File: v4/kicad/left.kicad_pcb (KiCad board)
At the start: 2 copper layers, 158.5 x 119.3 mm, 68 parts

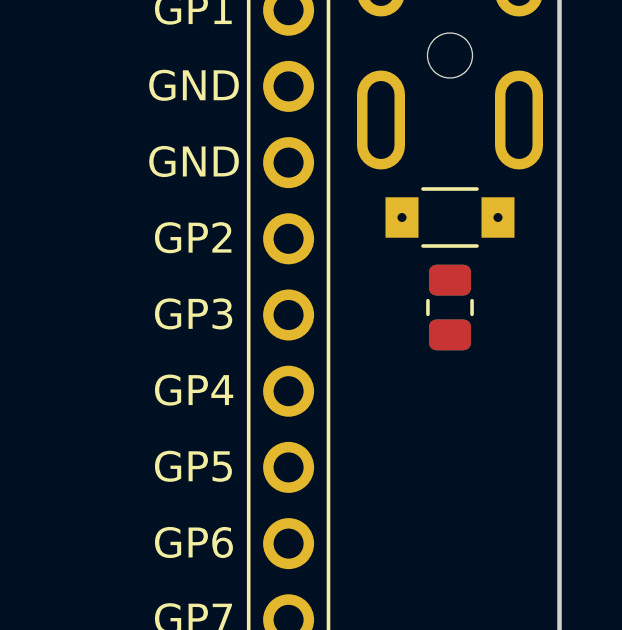
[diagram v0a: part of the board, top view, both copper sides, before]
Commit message: Finalize v4 TRRS protection placement clearance
Move data_resistor down 0.5mm (shift_y 15-17 -> 15-17.5, both halves) so
the TVS<->resistor courtyard gap is 0.67mm (was 0.17mm after the sod-123fl
land-pattern update grew the TVS courtyard). All clearances verified: TVS
0.75mm from the jack, ~28mm of open board below, both parts within the
outline. Regenerate and re-sync v4/kicad.
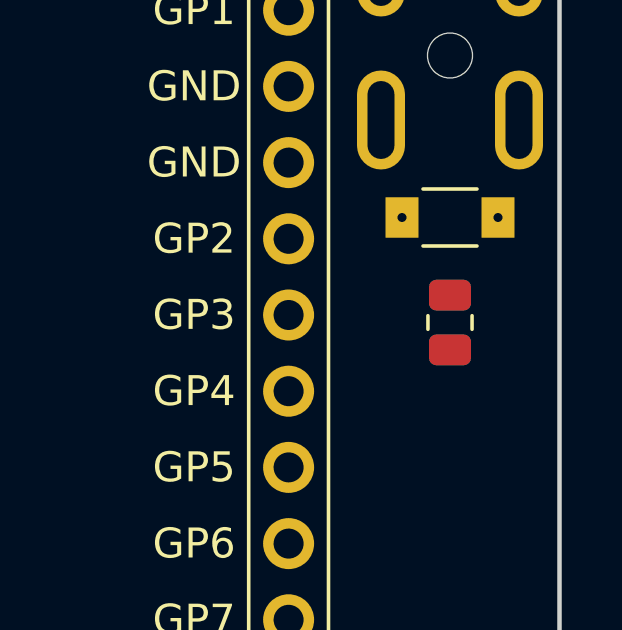
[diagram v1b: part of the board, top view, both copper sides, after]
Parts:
- moved SMD1 0.50 mm to (194.8, 118.0)

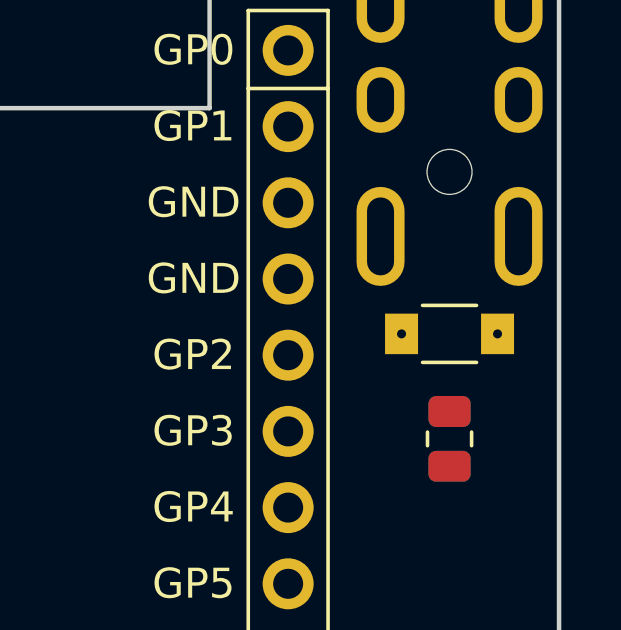
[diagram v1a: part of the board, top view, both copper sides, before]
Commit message: Label v4 TRRS protection parts descriptively
TVS (sod-123fl): name pads K (cathode/'to') and A (anode/'from') instead
of 1/2, set the value to SMF3.3CA, and document the params/pads in comments.
Resistor (smd_0805): override designator to R (R1, not the generic SMD1)
and add a '100R' silk value label. Document each part's pad->net mapping
in the ergogen config comments.
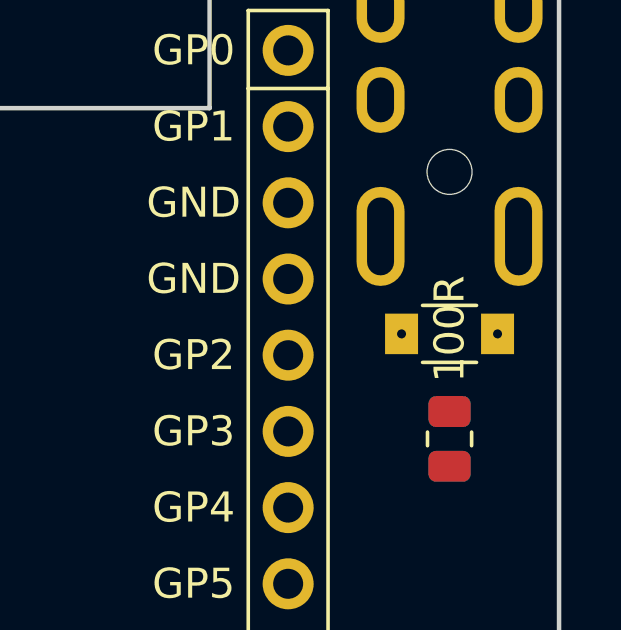
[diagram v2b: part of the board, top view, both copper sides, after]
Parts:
- removed SMD1: , smd_805
- added R1: , smd_805, F.Cu at (194.8, 118.0)
- D31: value SOD-123FL -> SMF3.3CA

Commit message: Sync v4 kicad working PCBs with finalized TRRS protection placement
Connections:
- TRRS1 pad 2: DATA_RAW -> GND
- TRRS1 pad 3: GND -> DATA_RAW

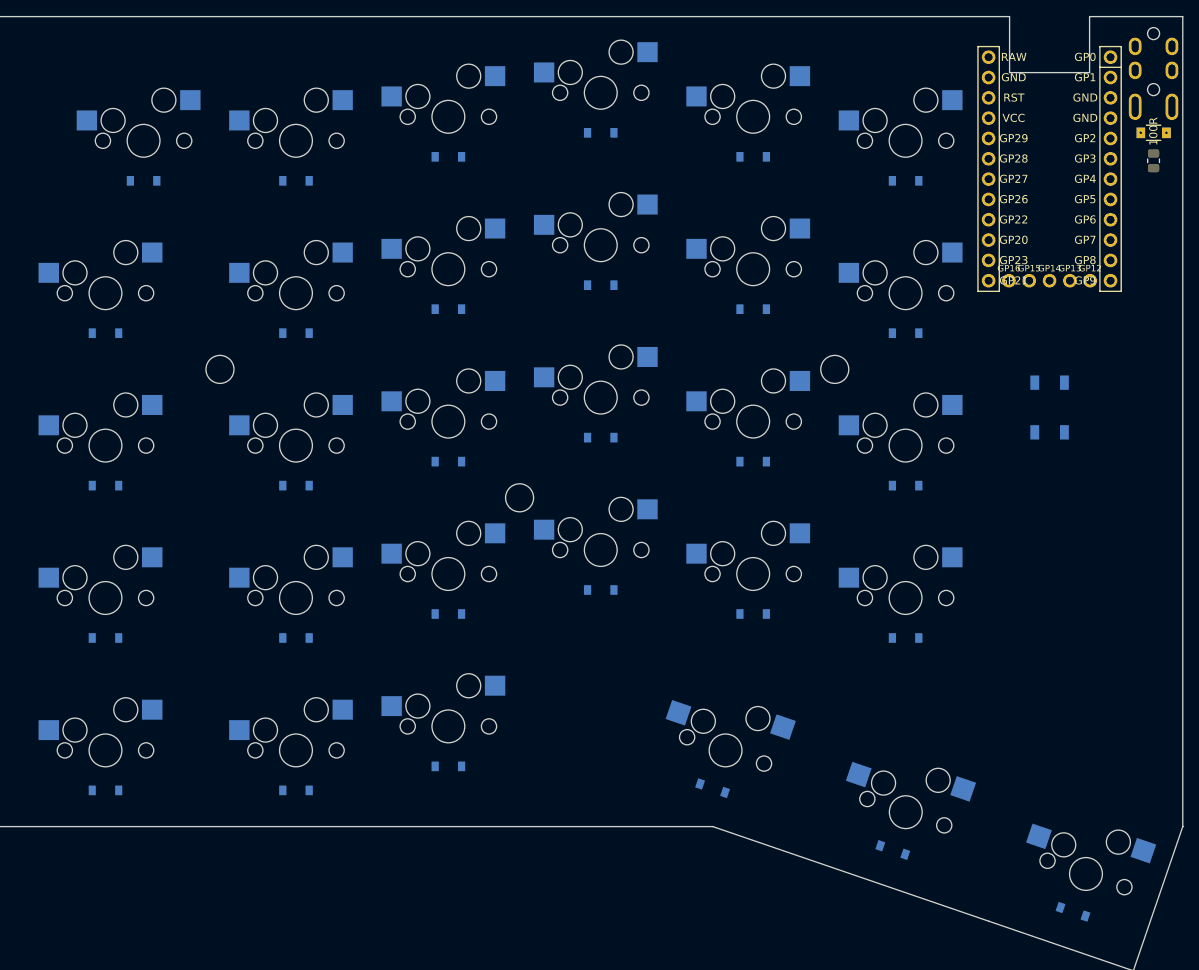
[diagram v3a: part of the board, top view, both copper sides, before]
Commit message: Tune v4 TRRS protection placement and update routed PCBs
Move data_tvs/data_resistor shifts (resistor to a ~2.38mm gap matching the MCU-TVS gap) on both halves, plus YAML formatting cleanup. Refresh left/right kicad PCBs.
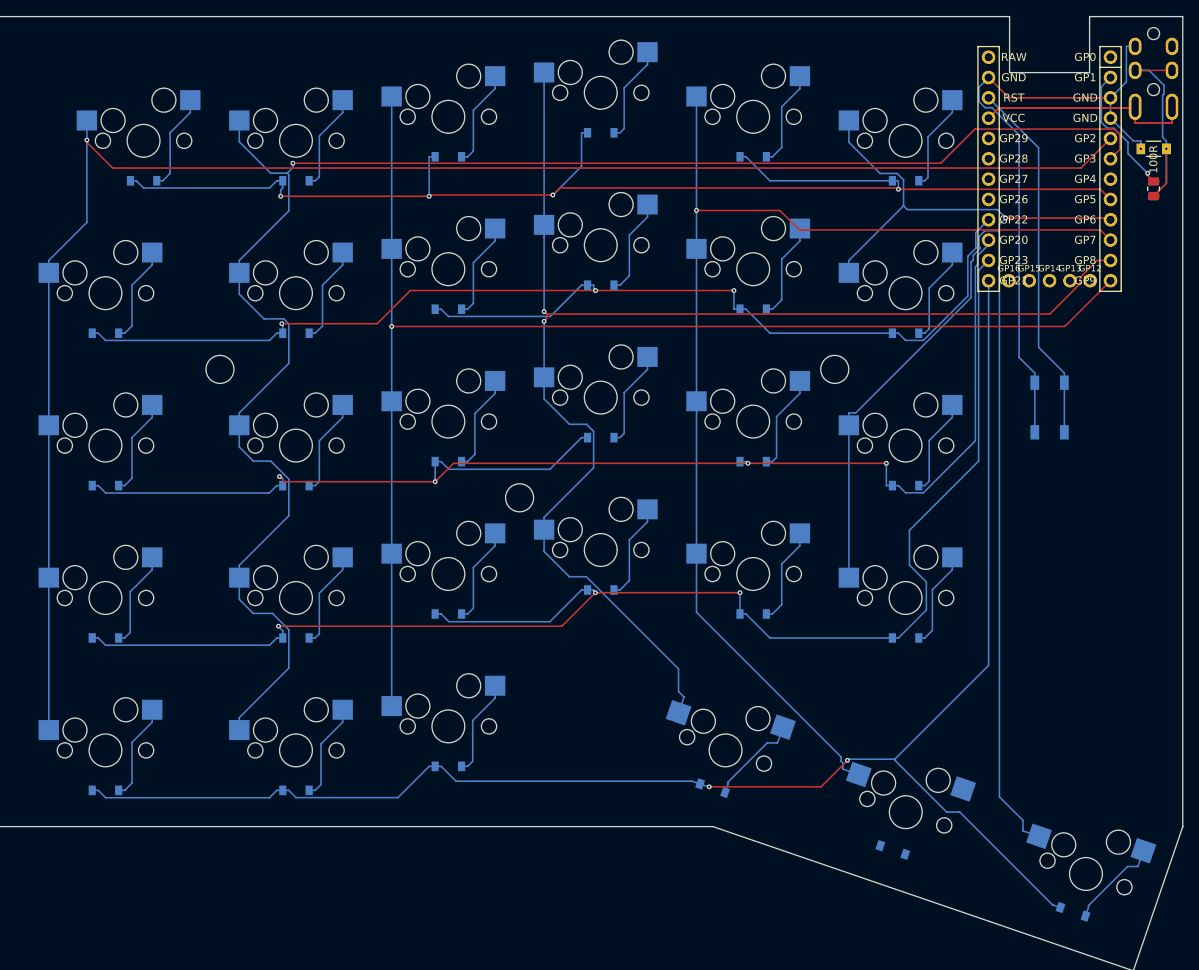
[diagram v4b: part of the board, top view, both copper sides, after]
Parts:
- moved R1 3.50 mm to (194.8, 121.5)
- moved D31 2.00 mm to (194.8, 116.5)
- turned D30 to -19 degrees
- turned D28 to -19 degrees
- turned D29 to -19 degrees
- turned S30 to -19 degrees
- turned S29 to -19 degrees
- turned S28 to -19 degrees
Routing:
- net P3: track 0.00 -> 212.5 mm, vias 0 -> 1
- net P2: track 0.00 -> 209.3 mm, vias 0 -> 1
- net P10: track 0.00 -> 198.4 mm, vias 0 -> 2
- net P6: track 0.00 -> 185.7 mm, vias 0 -> 1
- net P16: track 0.00 -> 185.3 mm, vias 0 -> 3
- net P14: track 0.00 -> 170.5 mm, vias 0 -> 4
- net P8: track 0.00 -> 169.0 mm, vias 0 -> 2
- net P9: track 0.00 -> 168.4 mm, vias 0 -> 1
- net P5: track 0.00 -> 164.4 mm, vias 0 -> 4
- net P15: track 0.00 -> 152.7 mm, vias 0 -> 3
- net P7: track 0.00 -> 147.1 mm, vias 0 -> 1
- net GND: track 0.00 -> 81.4 mm
- net RST: track 0.00 -> 45.7 mm
- net DATA_RAW: track 0.00 -> 30.3 mm
- net VCC: track 0.00 -> 27.5 mm
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
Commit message: Regenerate v4 PCBs and add routed masters with GND pour
Regenerate left/right working boards from the updated ergogen config and add the
v4/kicad/routed/ masters (the fab source), each carrying the B.Cu GND pour added
by copy-pcbs-kicad-to-routed.
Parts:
- moved B1 91.9 mm to (272.2, 132.4), turned to -90 degrees
- moved D28 91.2 mm to (230.1, 184.7), turned to -18.925 degrees
- moved D29 91.2 mm to (252.7, 192.5), turned to -18.925 degrees
- moved D30 91.2 mm to (275.2, 200.2), turned to -18.925 degrees
- moved D1 91.2 mm to (154.2, 185.0)
- moved D10 91.2 mm to (178.1, 108.8)
- moved D16 91.2 mm to (216.2, 159.9)
- moved D17 91.2 mm to (216.2, 140.9)
- moved D18 91.2 mm to (216.2, 121.8)
- moved D19 91.2 mm to (216.2, 102.8)
- moved D2 91.2 mm to (154.2, 165.9)
- moved D24 91.2 mm to (254.2, 165.9)
- moved D25 91.2 mm to (254.2, 146.9)
- moved D26 91.2 mm to (254.2, 127.8)
- moved D27 91.2 mm to (254.2, 108.8)
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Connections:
- net five_bottom renamed five_lower
- net five_meta renamed five_mod
- net five_number renamed five_num
- net five_top renamed five_upper
- net four_bottom renamed four_lower
- net four_meta renamed four_mod
- net four_number renamed four_num
- net four_top renamed four_upper
- net one_bottom renamed one_lower
- net one_meta renamed one_mod
- net one_number renamed one_num
- net one_top renamed one_upper
- net three_bottom renamed three_lower
- net three_meta renamed three_mod
- net three_number renamed three_num
- net three_top renamed three_upper
- net two_bottom renamed two_lower
- net two_meta renamed two_mod
- net two_number renamed two_num
- net two_top renamed two_upper
- net zero_bottom renamed zero_lower
- net zero_meta renamed zero_mod
- net zero_number renamed zero_num
- net zero_top renamed zero_upper
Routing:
- net P3: track 212.5 -> 0.00 mm, vias 1 -> 0
- net P2: track 209.3 -> 0.00 mm, vias 1 -> 0
- net P10: track 198.4 -> 0.00 mm, vias 2 -> 0
- net P6: track 185.7 -> 0.00 mm, vias 1 -> 0
- net P16: track 185.3 -> 0.00 mm, vias 3 -> 0
- net P14: track 170.5 -> 0.00 mm, vias 4 -> 0
- net P8: track 169.0 -> 0.00 mm, vias 2 -> 0
- net P9: track 168.4 -> 0.00 mm, vias 1 -> 0
- net P5: track 164.4 -> 0.00 mm, vias 4 -> 0
- net P15: track 152.7 -> 0.00 mm, vias 3 -> 0
- net P7: track 147.1 -> 0.00 mm, vias 1 -> 0
- net GND: track 81.4 -> 0.00 mm
- net RST: track 45.7 -> 0.00 mm
- net DATA_RAW: track 30.3 -> 0.00 mm
- net VCC: track 27.5 -> 0.00 mm
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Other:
- board size 158.5 x 119.3 mm -> 158 x 119 mm
- board text added: ""Splinter" keyboard v4 by @andornaut"
- board text added: "100R Panasonic ERJ-6ENF 1000V"
- board text added: "M3x0.5"
- board text added: "Reset switch E-Switch TL3342F450QG"
- board text added: "TRRS"
- board text added: "TVS Littelfuse SMF3.3CA"
- board text added: "https://github.com/andornaut/splinter-keyboard"
- board text added: "splitkb Liatris"

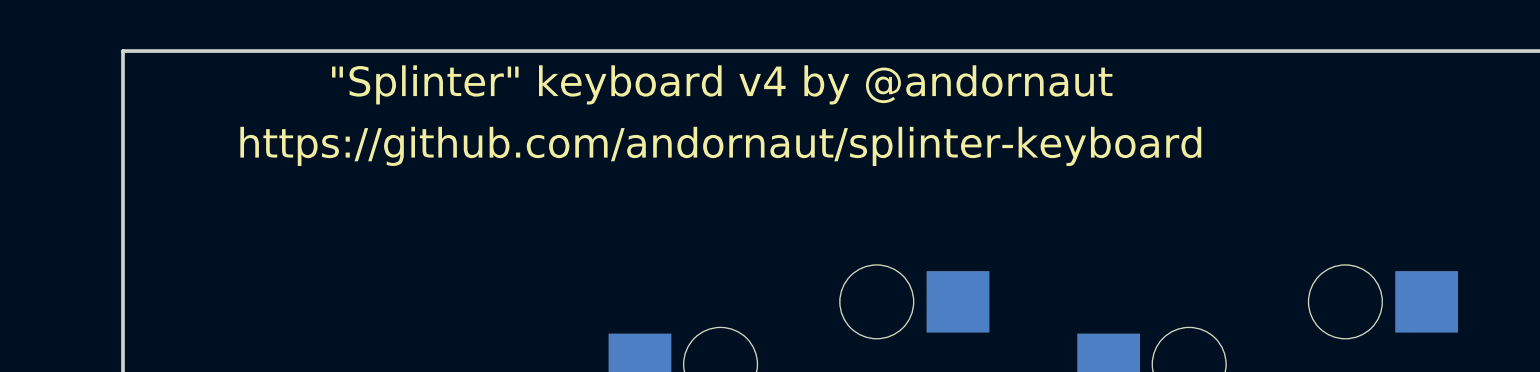
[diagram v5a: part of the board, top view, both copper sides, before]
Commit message: Switch fab pipeline to kicad-cli; add JLCPCB assembly (BOM/CPL)
- fab-jlcpcb.sh now exports gerbers/drill via kicad-cli (drop KiKit) and
  emits per-board BOM/CPL when v4/kicad/jlcpcb-parts.json exists
- Add gen-jlcpcb-bom-cpl.py and jlcpcb-parts.json (LCSC part assignment)
- Refactor v4 ergogen config: per-column/per-row mirror nets, single
  two-line credit text, shared placement x vars
- Regenerate v4 PCBs; update README for KiCad 10 / kicad-cli workflow
- Ignore KiCad .history/ local-history dir
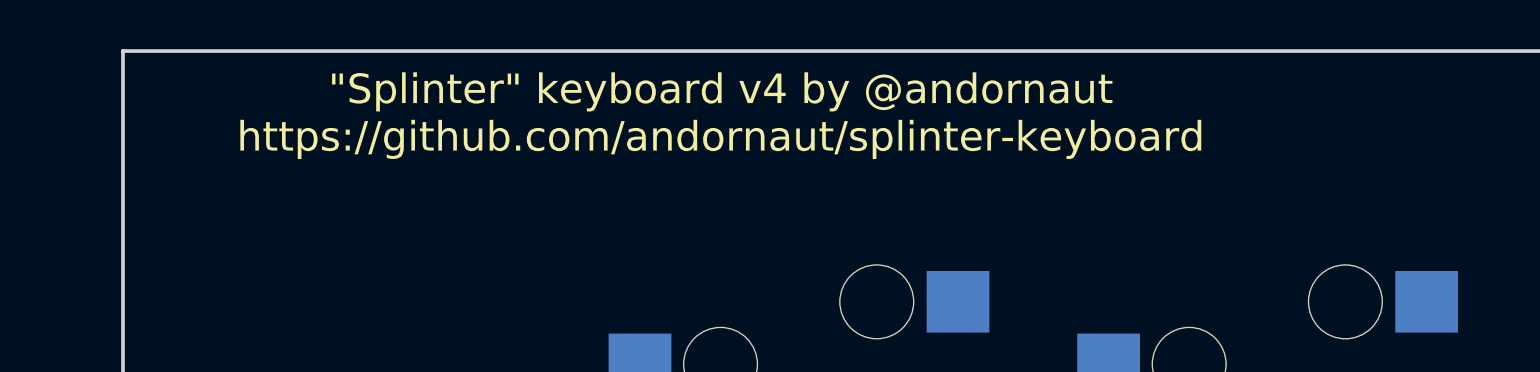
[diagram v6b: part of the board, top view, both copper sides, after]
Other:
- board text added: ""Splinter" keyboard v4 by @andornaut https://github.com/andornaut/splinter-keyboard"
- board text removed: ""Splinter" keyboard v4 by @andornaut"
- board text removed: "https://github.com/andornaut/splinter-keyboard"

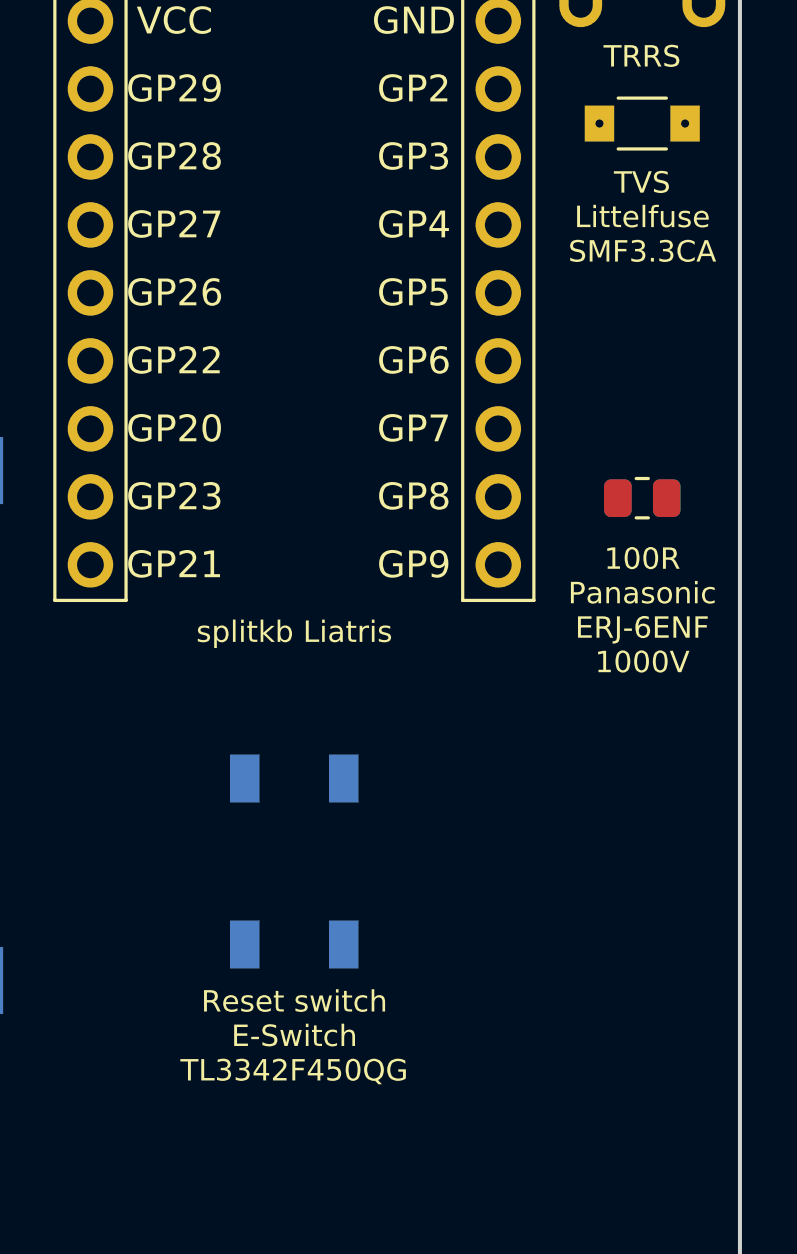
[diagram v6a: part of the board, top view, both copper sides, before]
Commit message: v4: switch data-line TVS to SMF5.0CA; refresh part labels and BOM
Change the data-line TVS from SMF3.3CA to SMF5.0CA (5V standoff) and
update its footprint, silk label, and jlcpcb-parts entry (C1851363).
Refresh reset/diode/resistor silk labels and BOM notes to match the
sourced parts, regenerate the v4 PCBs, and remove README references to
the uncommitted AGENTS.md.
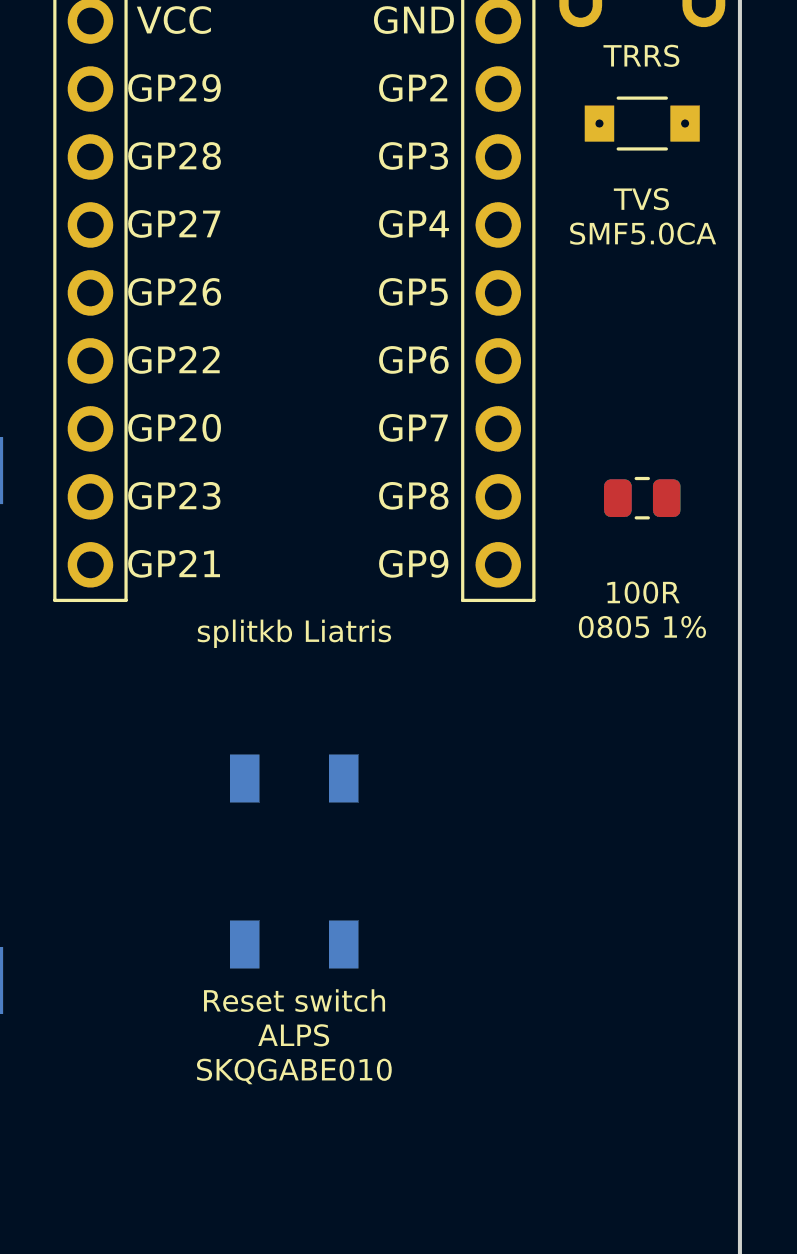
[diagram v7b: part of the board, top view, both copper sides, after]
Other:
- board text added: "100R 0805 1%"
- board text added: "Reset switch ALPS SKQGABE010"
- board text added: "TVS SMF5.0CA"
- board text removed: "100R Panasonic ERJ-6ENF 1000V"
- board text removed: "Reset switch E-Switch TL3342F450QG"
- board text removed: "TVS Littelfuse SMF3.3CA"
